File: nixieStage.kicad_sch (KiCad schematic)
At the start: 17 parts, among them Q601 PMBTA42, Q602 PMBTA42, Q603 PMBTA42, Q604 PMBTA42, Q605 PMBTA42, Q606 PMBTA42, Q607 PMBTA42, Q608 PMBTA42, Q609 PMBTA42, Q610 PMBTA42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

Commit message: add git hash
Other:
- title: (none) -> ZM108x, Z57x nixieboard
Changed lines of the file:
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@@
 (kicad_sch (version 20230121) (generator eeschema)
   (paper "A4")
+  (title_block
+    (title "ZM108x, Z57x nixieboard")
+    (date "2025-09-04")
+    (rev "3/${GITHASH}")
+    (comment 1 "Atuthor: Martin Sabol")
+  )
   (junction (at 129.54 121.92) (diameter 0) (color 0 0 0 0)
   )

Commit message: schema: bom: PNs update
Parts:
- C601: SPN CL10B105KO8NNNC -> CL21B105KOFNNNE
- Q601, Q602, Q603, Q604, Q605, Q606, Q607, Q608, Q609, Q610: SPN PMBTA42 -> PMBTA42,215
- R601, R602: SPN RC0603FR-073K3 -> RC0201FR-073K3L
- R603: SPN RC1206FR-0715K -> 1206S4F1502T5E
- U601: SPN 74HC595PW -> 74HC595PW,118
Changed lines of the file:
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@@
       (effects (font (size 1.27 1.27)) (justify left) hide)
     )
-    (property "SPN" "PMBTA42" (at 86.36 91.44 0)
+    (property "SPN" "PMBTA42,215" (at 86.36 91.44 0)
       (effects (font (size 1.27 1.27)) (justify left) hide)
     )
@@
       (effects (font (size 1.27 1.27)) (justify left) hide)
     )
-    (property "SPN" "PMBTA42" (at 106.68 91.44 0)
+    (property "SPN" "PMBTA42,215" (at 106.68 91.44 0)
       (effects (font (size 1.27 1.27)) (justify left) hide)
     )
@@
       (effects (font (size 1.27 1.27)) (justify left) hide)
     )
-    (property "SPN" "PMBTA42" (at 127 91.44 0)
+    (property "SPN" "PMBTA42,215" (at 127 91.44 0)
       (effects (font (size 1.27 1.27)) (justify left) hide)
     )
@@
       (effects (font (size 1.27 1.27)) (justify left) hide)
     )
-    (property "SPN" "PMBTA42" (at 147.32 91.44 0)
+    (property "SPN" "PMBTA42,215" (at 147.32 91.44 0)
       (effects (font (size 1.27 1.27)) (justify left) hide)
     )
@@
       (effects (font (size 1.27 1.27)) (justify left) hide)
     )
-    (property "SPN" "PMBTA42" (at 167.64 91.44 0)
+    (property "SPN" "PMBTA42,215" (at 167.64 91.44 0)
       (effects (font (size 1.27 1.27)) (justify left) hide)
     )
@@
       (effects (font (size 1.27 1.27)) (justify left) hide)
     )
-    (property "SPN" "PMBTA42" (at 187.96 91.44 0)
+    (property "SPN" "PMBTA42,215" (at 187.96 91.44 0)
       (effects (font (size 1.27 1.27)) (justify left) hide)
     )
@@
       (effects (font (size 1.27 1.27)) (justify left) hide)
     )
-    (property "SPN" "PMBTA42" (at 208.28 91.44 0)
+    (property "SPN" "PMBTA42,215" (at 208.28 91.44 0)
       (effects (font (size 1.27 1.27)) (justify left) hide)
     )
@@
       (effects (font (size 1.27 1.27)) (justify left) hide)
     )
-    (property "SPN" "PMBTA42" (at 228.6 91.44 0)
+    (property "SPN" "PMBTA42,215" (at 228.6 91.44 0)
       (effects (font (size 1.27 1.27)) (justify left) hide)
     )
@@
       (effects (font (size 1.27 1.27)) (justify left) hide)
     )
-    (property "SPN" "PMBTA42" (at 248.92 91.44 0)
+    (property "SPN" "PMBTA42,215" (at 248.92 91.44 0)
       (effects (font (size 1.27 1.27)) (justify left) hide)
     )
@@
       (effects (font (size 1.27 1.27)) (justify left) hide)
     )
-    (property "SPN" "PMBTA42" (at 269.24 91.44 0)
+    (property "SPN" "PMBTA42,215" (at 269.24 91.44 0)
       (effects (font (size 1.27 1.27)) (justify left) hide)
     )
@@
       (effects (font (size 1.27 1.27)) hide)
     )
-    (property "SPN" "74HC595PW" (at 57.15 127 0)
+    (property "SPN" "74HC595PW,118" (at 57.15 127 0)
       (effects (font (size 1.27 1.27)) hide)
     )
@@
       (effects (font (size 1.27 1.27)) hide)
     )
-    (property "SPN" "RC0603FR-073K3" (at 80.01 111.76 0)
+    (property "SPN" "RC0201FR-073K3L" (at 80.01 111.76 0)
       (effects (font (size 1.27 1.27)) hide)
     )
@@
       (effects (font (size 1.27 1.27)) hide)
     )
-    (property "SPN" "RC0603FR-073K3" (at 100.33 111.76 0)
+    (property "SPN" "RC0201FR-073K3L" (at 100.33 111.76 0)
       (effects (font (size 1.27 1.27)) hide)
     )
@@
       (effects (font (size 1.27 1.27)) hide)
     )
-    (property "SPN" "CL10B105KO8NNNC" (at 35.56 91.44 0)
+    (property "SPN" "CL21B105KOFNNNE" (at 35.56 91.44 0)
       (effects (font (size 1.27 1.27)) hide)
     )
@@
       (effects (font (size 1.27 1.27)) hide)
     )
-    (property "SPN" "RC1206FR-0715K" (at 163.83 41.91 0)
-      (effects (font (size 1.27 1.27)) hide)
-    )
+    (property "SPN" "1206S4F1502T5E" (at 163.83 41.91 0)
+      (effects (font (size 1.27 1.27)) hide)
+    )

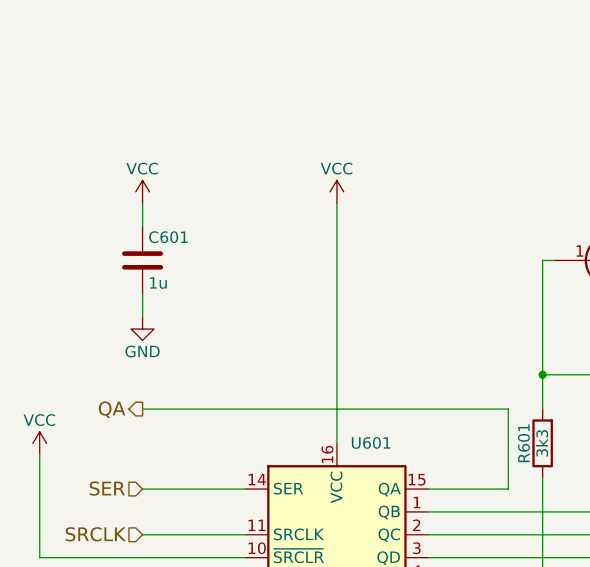
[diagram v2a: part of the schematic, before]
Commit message: BoM: optimize parts
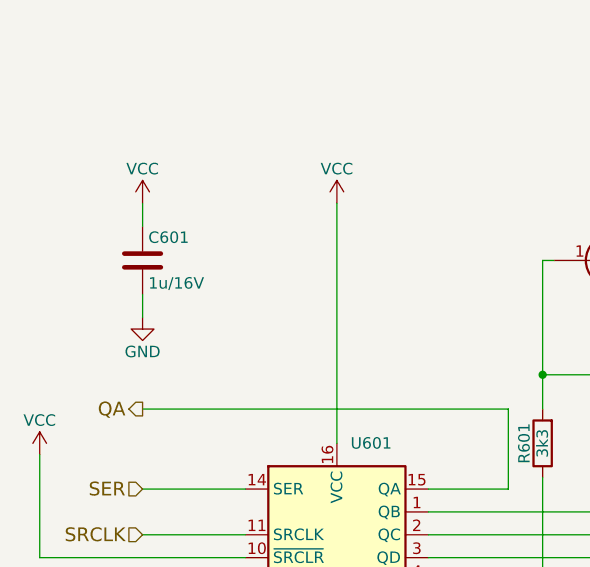
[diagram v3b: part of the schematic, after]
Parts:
- C601: value 1u -> 1u/16V
- R601, R602: SPN RC0201FR-073K3L -> 0603SAF3301T5E
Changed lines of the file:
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@@
       (effects (font (size 1.27 1.27)) hide)
     )
-    (property "SPN" "RC0201FR-073K3L" (at 80.01 111.76 0)
+    (property "SPN" "0603SAF3301T5E" (at 80.01 111.76 0)
       (effects (font (size 1.27 1.27)) hide)
     )
@@
       (effects (font (size 1.27 1.27)) hide)
     )
-    (property "SPN" "RC0201FR-073K3L" (at 100.33 111.76 0)
+    (property "SPN" "0603SAF3301T5E" (at 100.33 111.76 0)
       (effects (font (size 1.27 1.27)) hide)
     )
@@
       (effects (font (size 1.27 1.27)) (justify left))
     )
-    (property "Value" "1u" (at 36.195 93.98 0)
+    (property "Value" "1u/16V" (at 36.195 93.98 0)
       (effects (font (size 1.27 1.27)) (justify left))
     )
